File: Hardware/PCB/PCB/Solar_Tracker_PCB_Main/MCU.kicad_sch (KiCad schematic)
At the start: 22 parts, among them IC1 ESP32-S3-WROOM-1-N4R8, IC5 LM1117MPX-3.3_NOPB, J1 1729076, J2 USB4940-00-A, J3 1729076, J4 1977223-1, J5 1977223-1, J6 1729076

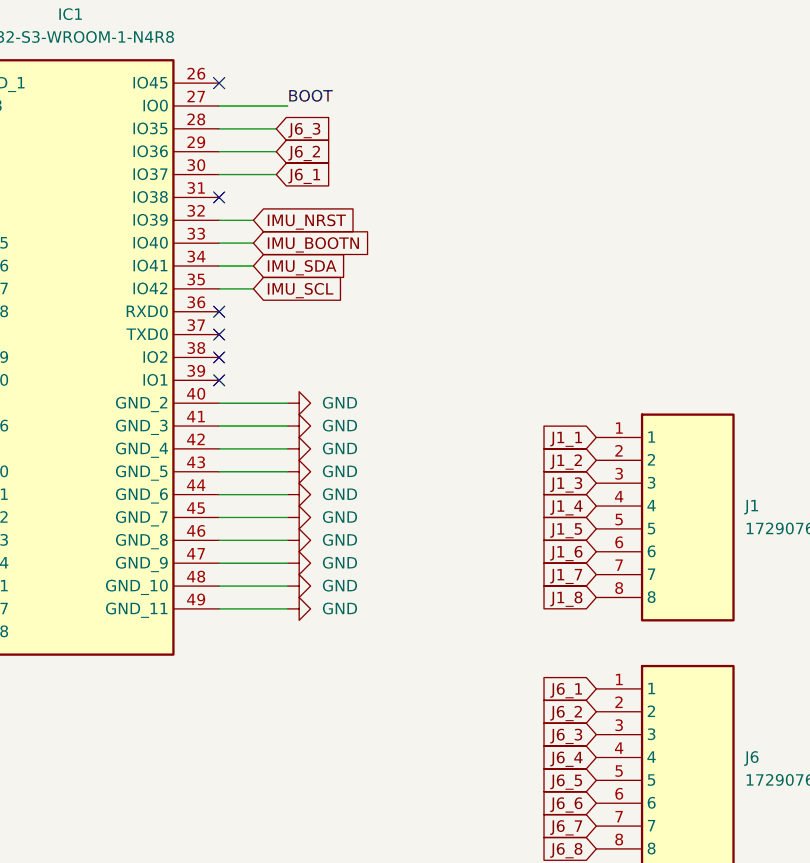
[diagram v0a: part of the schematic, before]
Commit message: Agregar tierra a las Borneras
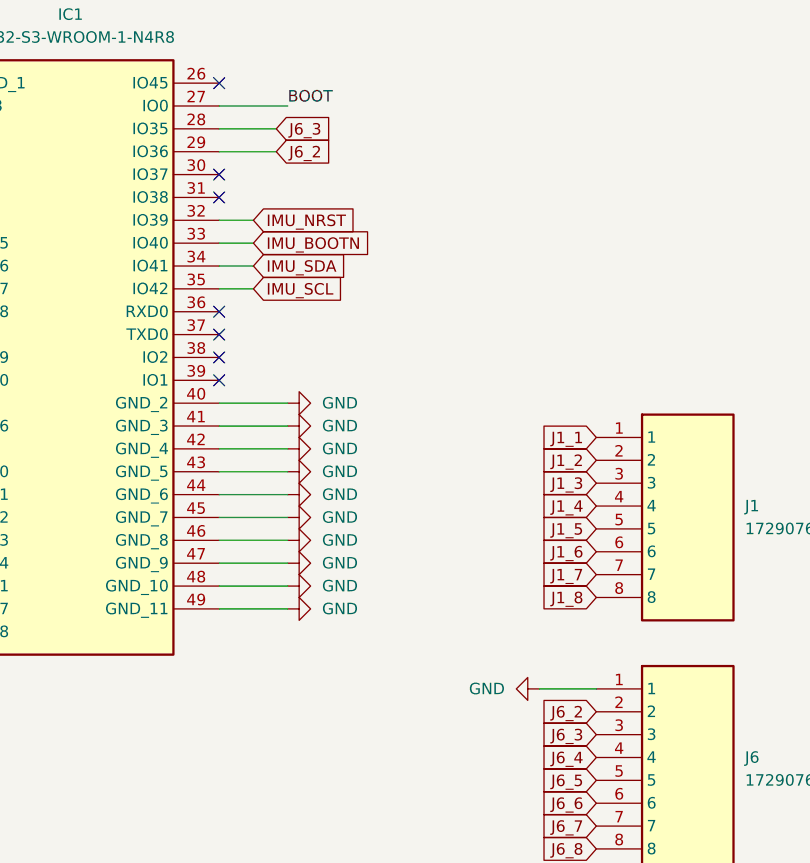
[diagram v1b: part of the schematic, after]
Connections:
- net GND: now also J6.1
- net J6_1: no longer names the net of IC1.30 (IO37)
- net J6_1: no longer J6.1
- no-connect marks 10 -> 11
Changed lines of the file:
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@@
 	)
 	(no_connect
+		(at 107.95 107.95)
+	)
+	(no_connect
 		(at 107.95 125.73)
 	)
@@
 	(wire
 		(pts
-			(xy 72.39 151.13) (xy 74.93 151.13)
+			(xy 143.51 165.1) (xy 149.86 165.1)
 		)
 		(stroke
@@
 	(wire
 		(pts
-			(xy 107.95 107.95) (xy 114.3 107.95)
+			(xy 72.39 151.13) (xy 74.93 151.13)
 		)
 		(stroke
@@
 		)
 	)
-	(global_label "J6_1"
-		(shape input)
-		(at 114.3 107.95 0)
-		(fields_autoplaced yes)
-		(effects
-			(font
-				(size 1.27 1.27)
-			)
-			(justify left)
-		)
-		(property "Intersheetrefs" "${INTERSHEET_REFS}"
-			(at 121.6394 107.95 0)
-			(effects
-				(font
-					(size 1.27 1.27)
-				)
-				(justify left)
-				(hide yes)
-			)
-		)
-	)
 	(global_label "J1_7"
 		(shape input)
@@
 		)
 	)
-	(global_label "J6_1"
-		(shape input)
-		(at 149.86 165.1 180)
-		(fields_autoplaced yes)
-		(effects
-			(font
-				(size 1.27 1.27)
-			)
-			(justify right)
-		)
-		(property "Intersheetrefs" "${INTERSHEET_REFS}"
-			(at 142.5206 165.1 0)
-			(effects
-				(font
-					(size 1.27 1.27)
-				)
-				(justify right)
-				(hide yes)
-			)
-		)
-	)
 	(global_label "J6_2"
 		(shape input)
@@
 					(unit 1)
 				)
+			)
+		)
+	)
+	(symbol
+		(lib_id "power:GND")
+		(at 143.51 165.1 270)
+		(unit 1)
+		(exclude_from_sim no)
+		(in_bom yes)
+		(on_board yes)
+		(dnp no)
+		(fields_autoplaced yes)
+		(property "Reference" "#PWR074"
+			(at 137.16 165.1 0)
+			(effects
+				(font
+					(size 1.27 1.27)
+				)
+				(hide yes)
+			)
+		)
+		(property "Value" "GND"
+			(at 139.7 165.0999 90)
+			(effects
+				(font
+					(size 1.27 1.27)
+				)
+				(justify right)
+			)
+		)
+		(property "Footprint" ""
+			(at 143.51 165.1 0)
+			(effects
+				(font
+					(size 1.27 1.27)
+				)
+				(hide yes)
+			)
+		)
+		(property "Datasheet" ""
+			(at 143.51 165.1 0)
+			(effects
+				(font
+					(size 1.27 1.27)
+				)
+				(hide yes)
+			)
+		)
+		(property "Description" "Power symbol creates a global label with name \"GND\" , ground"
+			(at 143.51 165.1 0)
+			(effects
+				(font
+					(size 1.27 1.27)
+				)
+				(hide yes)
+			)
+		)
+		(pin "1"
+		)
+		(instances
+			(project "Solar_Tracker_PCB_Main"
+				(path "/99b6ddd9-7ffe-4c85-972a-e0f594a166d4/521ed49f-67a8-4f65-9cb7-064f532bae28"
+					(reference "#PWR074")
+					(unit 1)
+				)

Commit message: Agregue conectores JST
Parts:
- removed J1, J3, J6: 1729076, 1729076:1729076, symbol 1729076:1729076
- added J1, J8, J9: SM08B-SRSS-TB_LF__SN_, SM08B:SM08BSRSSTBLFSN, symbol SM08B-SRSS-TB_LF__SN_:SM08B-SRSS-TB_LF__SN_
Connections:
- net GND: now also J1.10 (MP2), J1.2, J1.4, J1.6, J1.8, J1.9 (MP1), J8.10 (MP2), J8.8, J8.9 (MP1), J9.10 (MP2), J9.8, J9.9 (MP1)
- net J1_2: now also J8.7
- net J1_3: now also J8.6
- net J1_4: now also J8.5
- net J1_5: now also J8.4
- net J1_6: now also J8.3
- net J1_7: now also J8.2
- net J1_8: now also J8.1
- net J6_2: now also J9.2
- net J6_3: now also J9.3
- net J6_4: now also J9.4
- net J6_5: now also J9.5
- net J6_6: now also J9.6
- net J6_7: now also J9.7
- net SL_INT: now also J1.7
- net SL_SCL: now also J1.3
- net SL_SDA: now also J1.5
- net VDD: now also J1.1
- net J1_1 renamed J6_1
- net J6_1: now also J9.1
- net J6_8: no longer names the net of IC1.23 (IO21)
- no-connect marks 11 -> 12
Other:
- moved on the sheet: C22

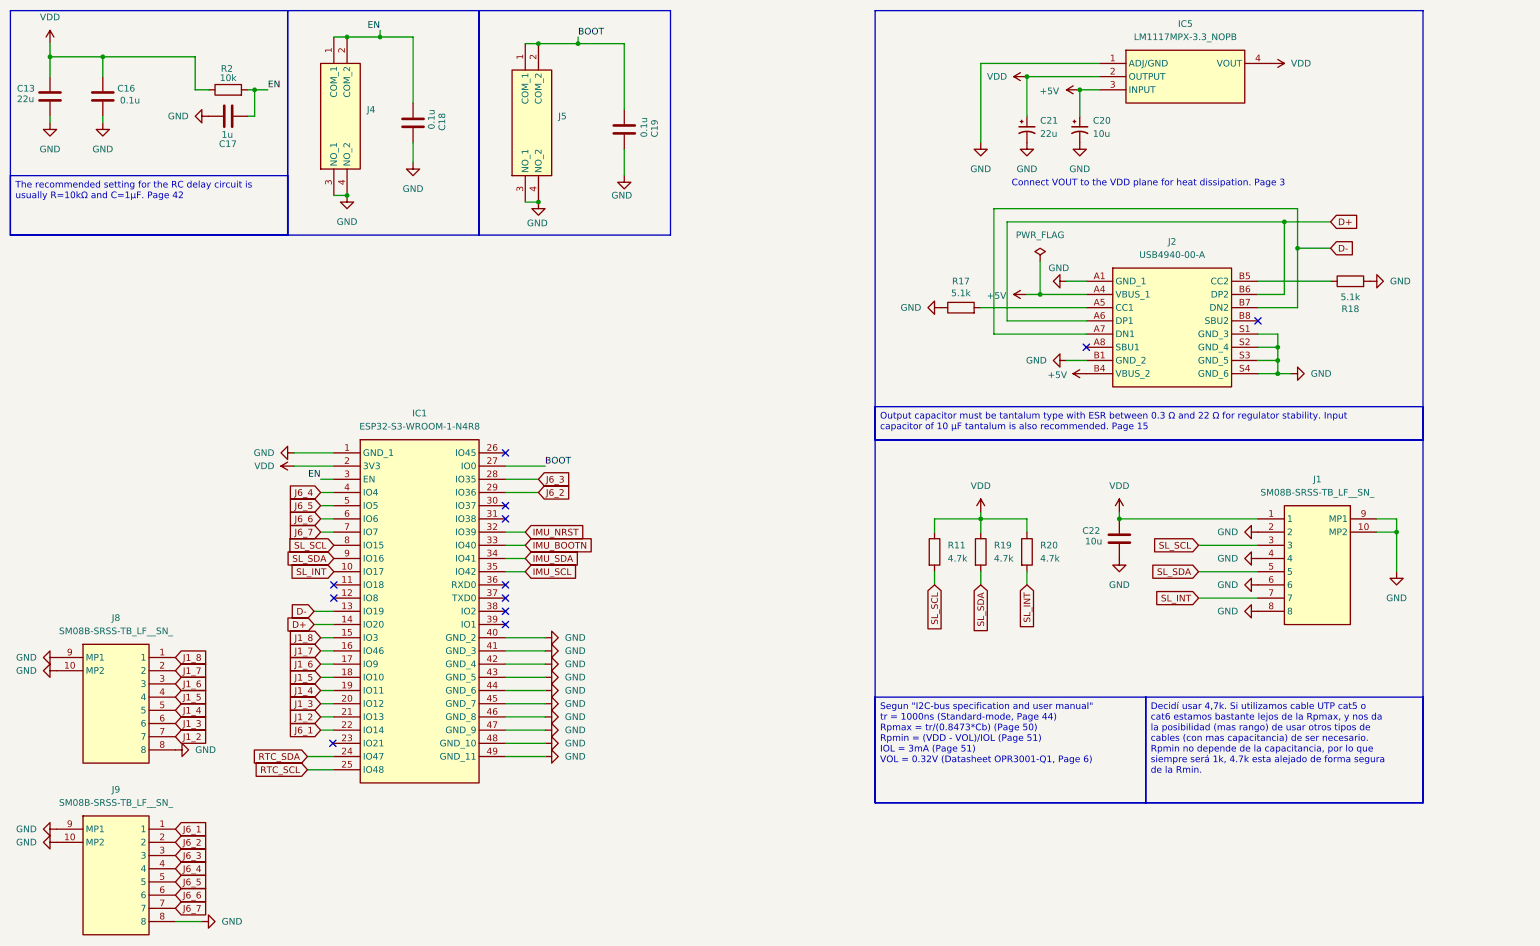
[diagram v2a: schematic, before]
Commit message: Agregue protecciones de polaridad inversa y independencia de fuentes
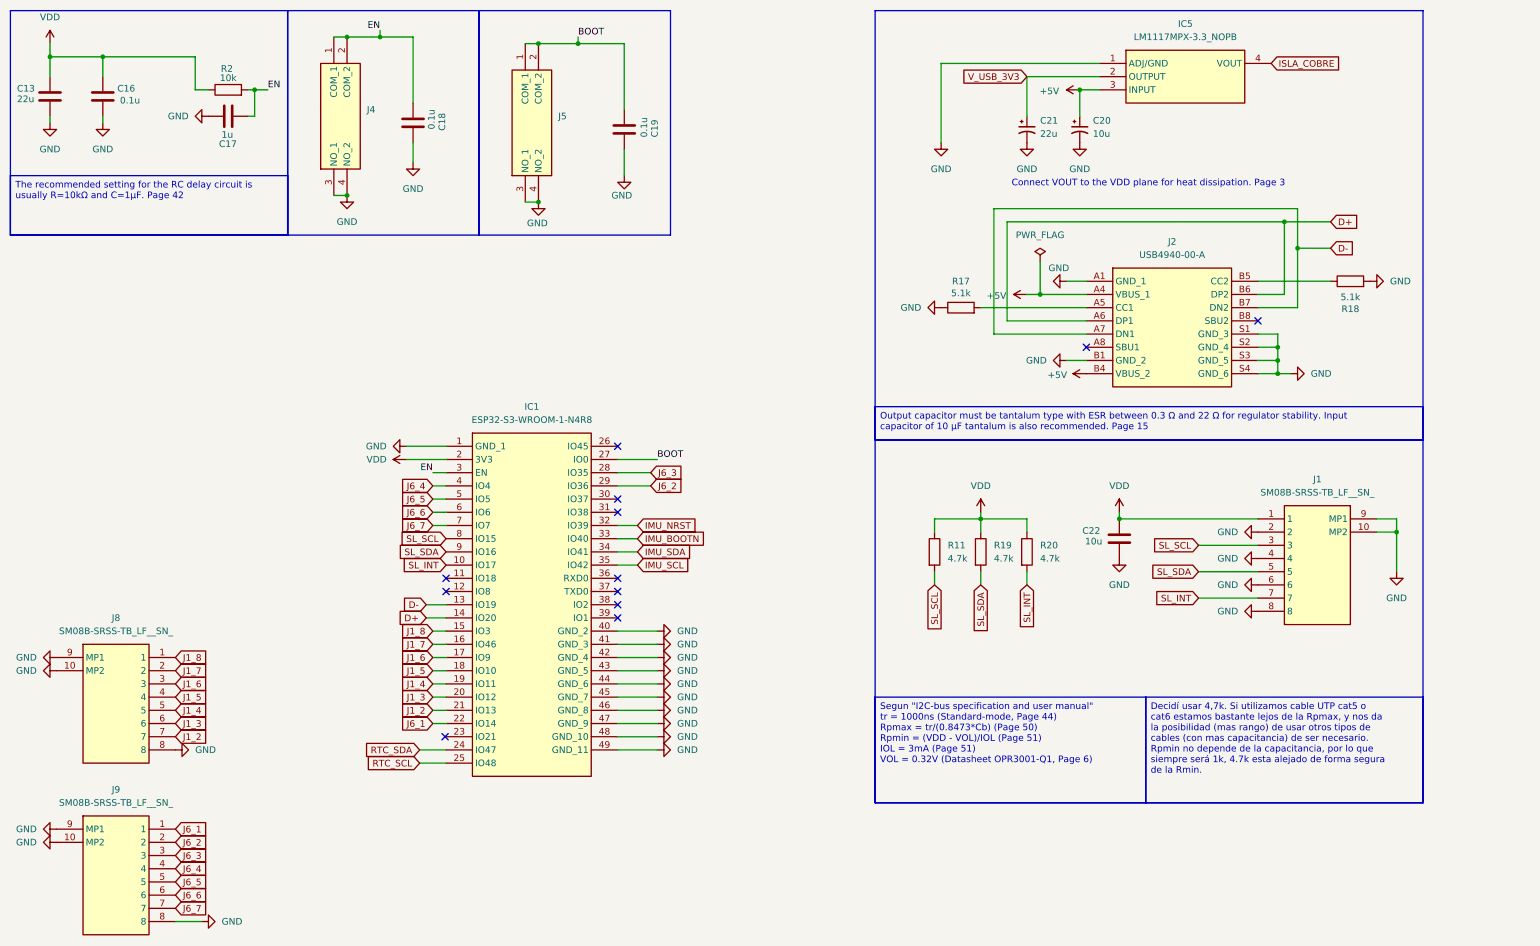
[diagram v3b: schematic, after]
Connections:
- net VDD: no longer C21.1, IC5.2 (OUTPUT), IC5.4 (VOUT)
- new net ISLA_COBRE: IC5.4 (VOUT)
- new net V_USB_3V3: C21.1, IC5.2 (OUTPUT)
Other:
- moved on the sheet: IC1
